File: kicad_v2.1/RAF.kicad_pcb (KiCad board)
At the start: 2 copper layers, 68.6 x 53.3 mm, 40 parts, among them J1 SERVO, J2 SERVO, J3 SOL, J4 SERVO, J5 PUMP, J6 WS2811-OUT, J7 I2C, P1 Power, P2 Analog, P3 Digital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

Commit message: RAF v2.1 kicad layout
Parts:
- D1, D2: value SD3220 -> S1ATR
- moved C2 6.84 mm to (151.6, 92.1), turned to 90 degrees
- moved U2 6.40 mm to (150.4, 102.9)
- moved R5 5.12 mm to (165.6, 94.0)
- moved R6 5.12 mm to (165.6, 97.8)
- moved R7 5.12 mm to (165.6, 90.2)
- moved C1 4.58 mm to (147.8, 92.1), turned to 90 degrees
- moved Q1 4.49 mm to (171.3, 96.5)
- moved J1 3.81 mm to (168.1, 80.6)
- moved J2 3.81 mm to (165.6, 80.6)
- moved J4 3.81 mm to (163.1, 80.6)
- moved JP4 3.50 mm to (137.7, 109.9)
- moved JP3 3.50 mm to (137.7, 111.8)
- moved JP2 3.49 mm to (137.7, 113.7)
- moved JP1 3.49 mm to (137.7, 115.6)
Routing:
- net GND: track 0.00 -> 194.5 mm, vias 0 -> 14
- net +5V: track 0.00 -> 156.4 mm
- net /A3: track 0.00 -> 68.6 mm, vias 0 -> 1
- net /SVCC: track 0.00 -> 66.0 mm, vias 0 -> 1
- net /Vin: track 0.00 -> 59.9 mm, vias 0 -> 1
- net /A2: track 0.00 -> 56.3 mm
- net /9(**): track 0.00 -> 55.3 mm
- net /A1: track 0.00 -> 53.5 mm, vias 0 -> 1
- net /A0: track 0.00 -> 50.6 mm, vias 0 -> 1
- net /12(MISO): track 0.00 -> 42.3 mm
- net Net-(D1-Pad2): track 0.00 -> 29.2 mm
- net /8: track 0.00 -> 26.5 mm
- net /2: track 0.00 -> 24.6 mm
- net Net-(D2-Pad2): track 0.00 -> 17.5 mm
- net /A5(SCL): track 0.00 -> 15.5 mm
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- added copper zone on B.Cu, net GND
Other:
- board text added: "Ready Aim Fire V2.1"
- board text removed: "Ready Aim Fire V3.0"

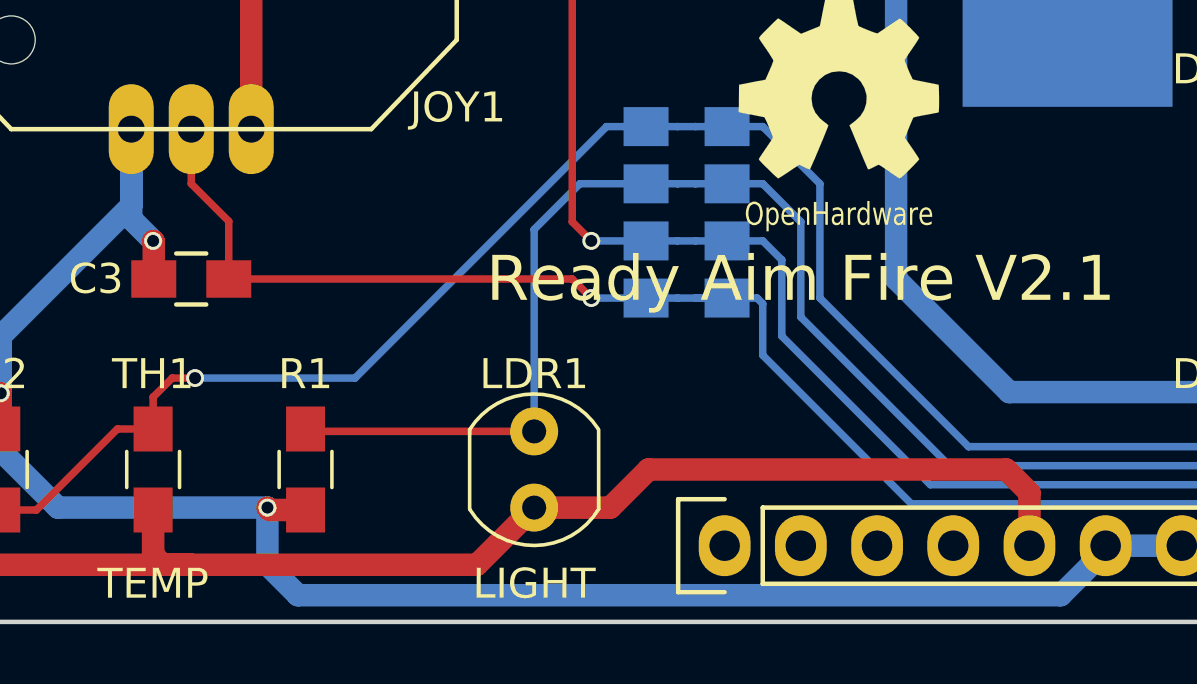
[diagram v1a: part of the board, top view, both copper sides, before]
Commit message: LDR footprint modified
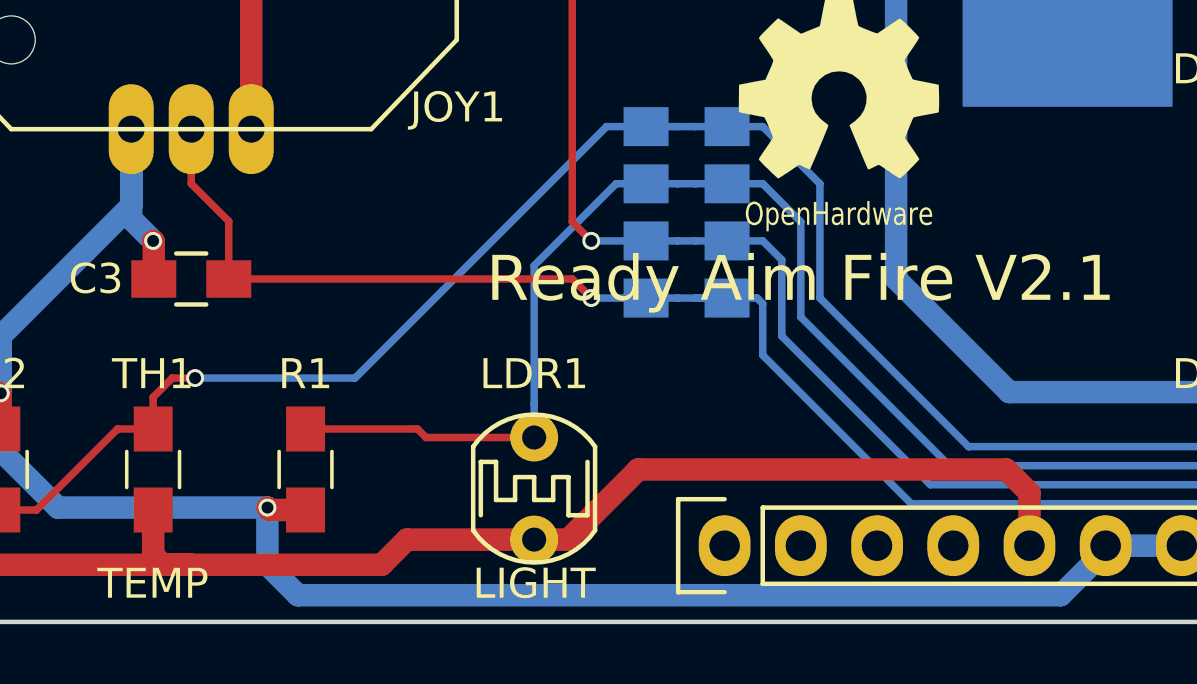
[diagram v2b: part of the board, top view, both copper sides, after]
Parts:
- LDR1: footprint RAF_Libs:Resistor_LDR_4.9x4.2_RM2.54 -> RAF_Libs:Resistor_LDR_5.0x3.4
- moved LDR1 0.64 mm to (132.6, 121.9)

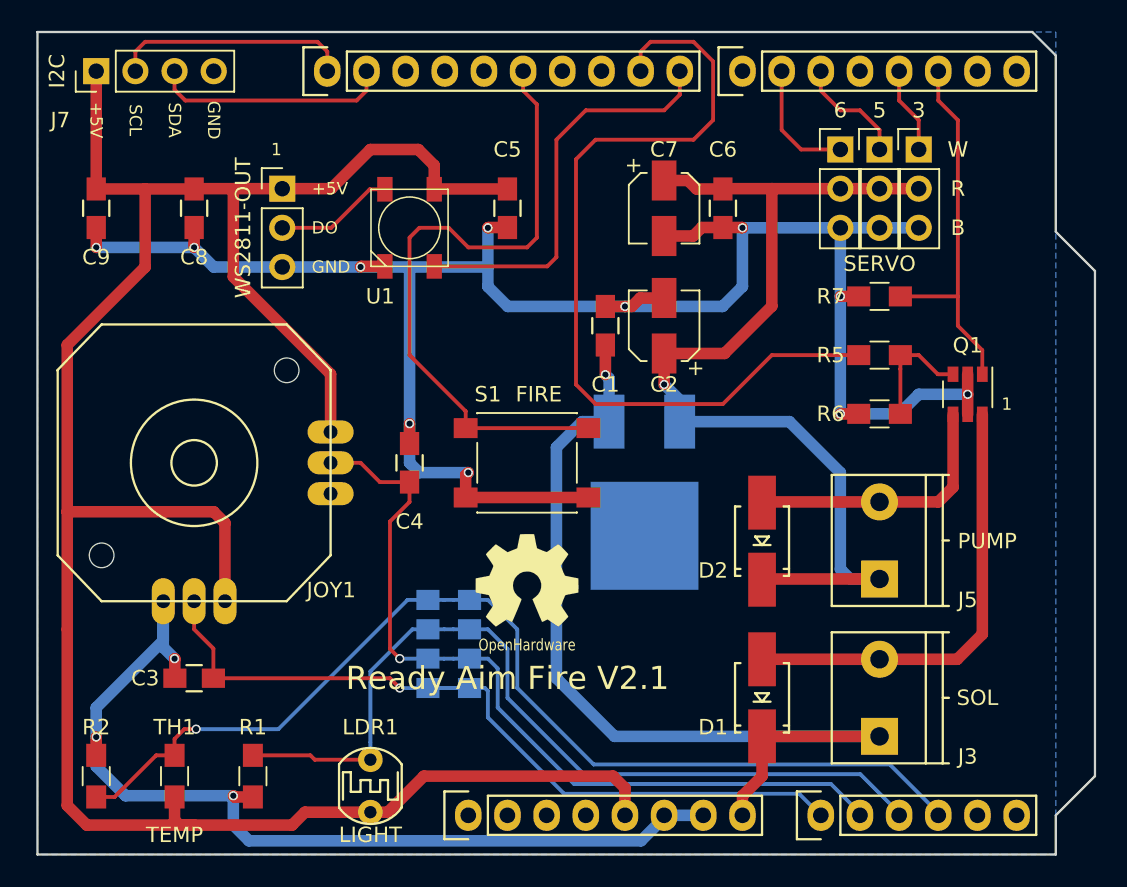
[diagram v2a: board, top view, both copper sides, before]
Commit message: PCB ver2.1 complete, added variable resistor for LDR
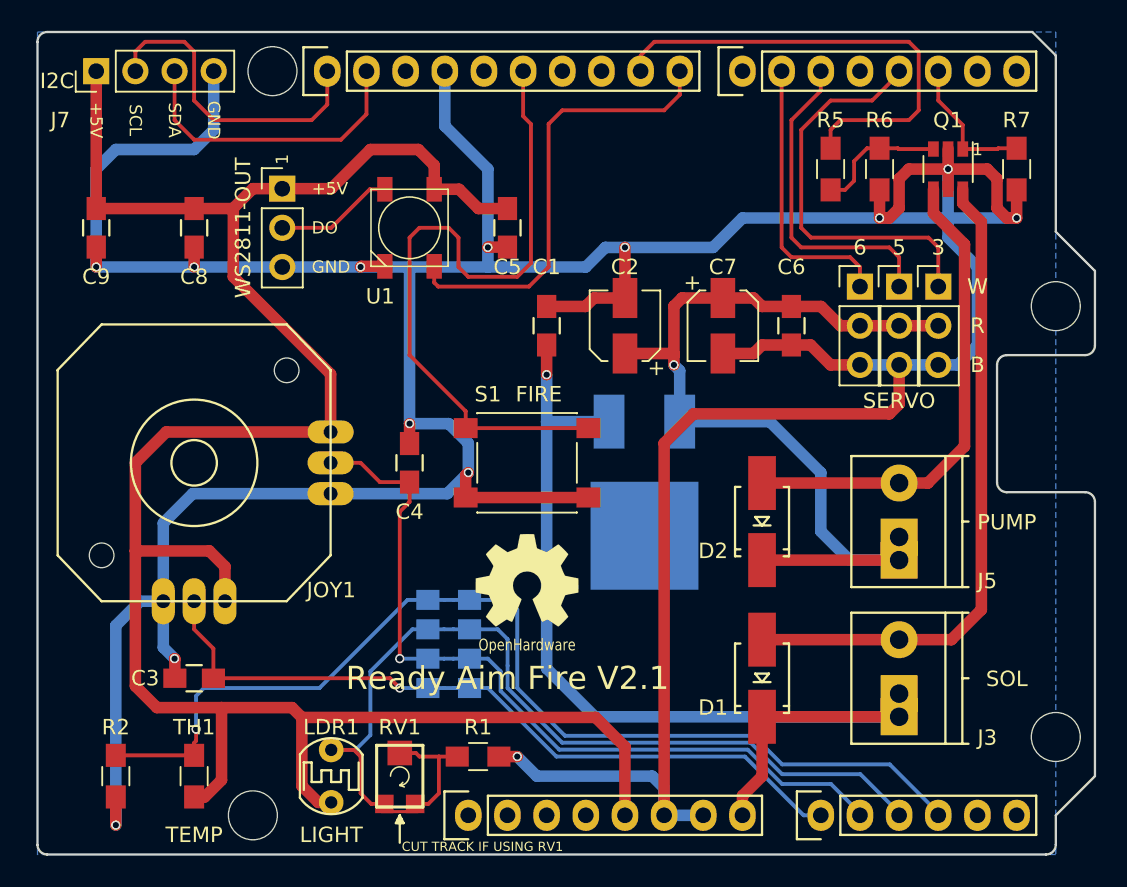
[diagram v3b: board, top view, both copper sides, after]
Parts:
- added H1: NPTH_hole, RAF_Libs:NPTH_hole_3mm, F.Cu at (125.0, 123.8)
- added H2: NPTH_hole, RAF_Libs:NPTH_hole_3mm, F.Cu at (177.0, 118.7)
- added H3: NPTH_hole, RAF_Libs:NPTH_hole_3mm, F.Cu at (177.0, 90.8)
- added H4: NPTH_hole, RAF_Libs:NPTH_hole_3mm, F.Cu at (126.2, 75.6)
- added RV1: 100k, RAF_Libs:Res_variable, F.Cu at (134.5, 121.3)
- R7: value 100K -> 100k
- moved R6 15.9 mm to (165.6, 81.9), turned to 90 degrees
- moved R1 14.7 mm to (139.6, 120.0), turned to 0 degrees
- moved Q1 14.7 mm to (170.1, 81.9)
- moved R5 12.5 mm to (162.4, 81.9), turned to 90 degrees
- moved R7 12.1 mm to (174.5, 81.9), turned to 90 degrees
- moved J1 8.98 mm to (169.4, 89.5)
- moved J2 8.98 mm to (166.9, 89.5)
- moved J4 8.98 mm to (164.3, 89.5)
- moved C6 8.82 mm to (159.9, 92.1)
- moved C7 8.52 mm to (155.4, 92.1)
- moved C1 3.81 mm to (144.0, 92.1)
- moved LDR1 2.62 mm to (130.0, 121.3)
- moved C2 2.54 mm to (149.1, 92.1)
- moved WYO1 2.54 mm to (125.0, 118.7)
- moved J3 1.80 mm to (166.9, 114.9)
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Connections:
- R1 pad 1: /A2 -> Net-(R1-Pad1)
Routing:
- net GND: track 194.5 -> 293.9 mm, vias 14 -> 13
- net /9(**): track 55.3 -> 30.9 mm
- net /3(**): track 5.61 -> 26.3 mm
- net /2: track 24.6 -> 9.22 mm
- net Net-(D2-Pad2): track 17.5 -> 31.6 mm
- net /5(**): track 7.40 -> 21.0 mm
- net Net-(D1-Pad2): track 29.2 -> 42.8 mm
- net +5V: track 156.4 -> 144.8 mm
- net /6(**): track 8.15 -> 18.3 mm
- net Net-(R1-Pad1): track 0.00 -> 8.03 mm
- net /Vin: track 59.9 -> 66.5 mm
- net /SVCC: track 66.0 -> 59.6 mm
- net /A5(SCL): track 15.5 -> 20.5 mm
- net /A4(SDA): track 15.5 -> 19.6 mm
- net /12(MISO): track 42.3 -> 45.4 mm
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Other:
- outline, holes or cut-outs redrawn
- board text added: "CUT TRACK IF USING RV1"

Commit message: kicad_v2.1 updated silkscreen
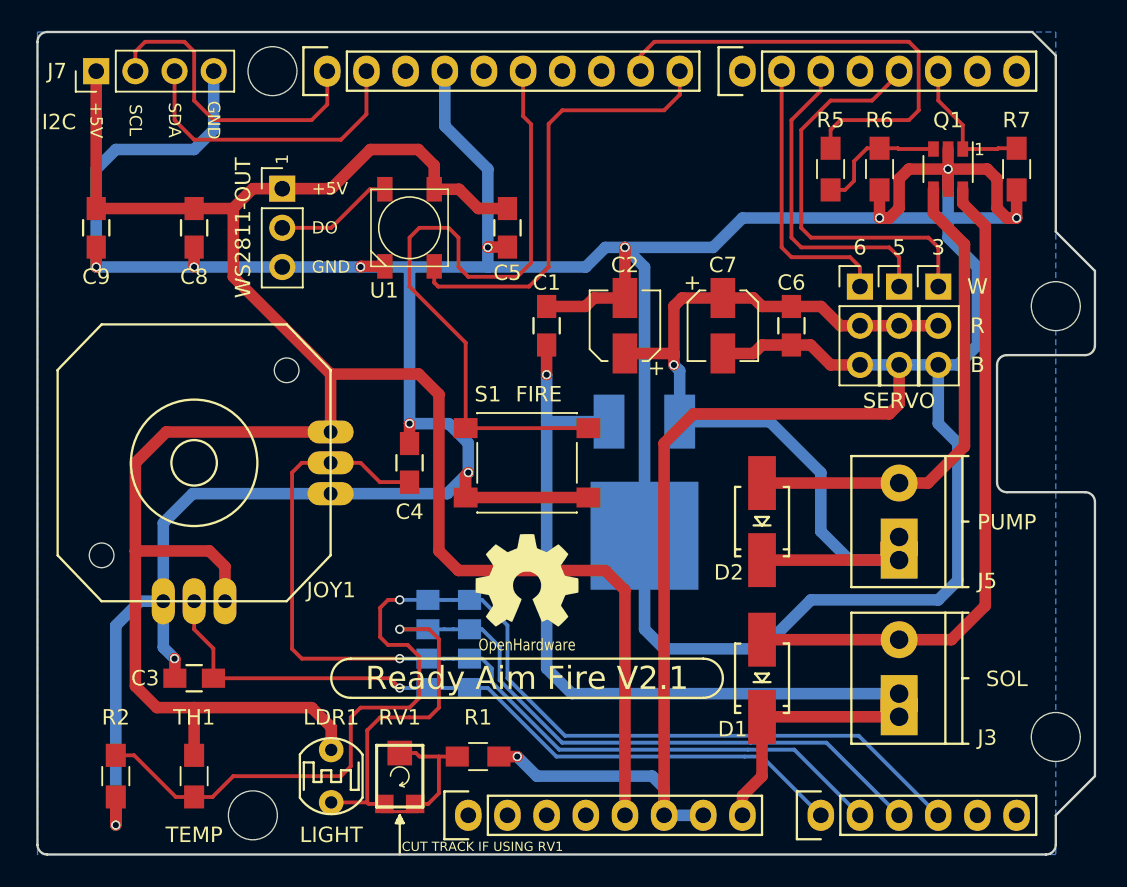
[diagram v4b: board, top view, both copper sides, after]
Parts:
- moved WYO1 3.70 mm to (126.9, 115.6)
- turned LDR1 to 270 degrees
- turned TH1 to 270 degrees
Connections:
- R1 pad 1: Net-(R1-Pad1) -> /A2
- RV1 pad 2: Net-(R1-Pad1) -> /A2
- RV1 pad 3: Net-(R1-Pad1) -> /A2
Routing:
- net GND: track 293.9 -> 356.4 mm
- net /A2: track 55.8 -> 70.1 mm, vias 0 -> 1
- net +5V: track 144.8 -> 157.1 mm
- net /A1: track 52.3 -> 61.9 mm
- net /A3: track 68.8 -> 77.4 mm
- net Net-(R1-Pad1): track 8.03 -> 0.00 mm
- net /Vin: track 66.5 -> 65.9 mm
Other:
- net class 0.12 added: clearance 0.2, trace_width 0.12, via_dia 0.6, via_drill 0.4
- rule trace_min: 0.2 -> 0.1
